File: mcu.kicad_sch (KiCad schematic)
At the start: 30 parts, among them J301 CONN_MCU_SERIAL, J302 EXT_CONN, SW301 SW_RST, SW302 SW_BOOT0, U301 STM32F765IITx, Y301 25MHz

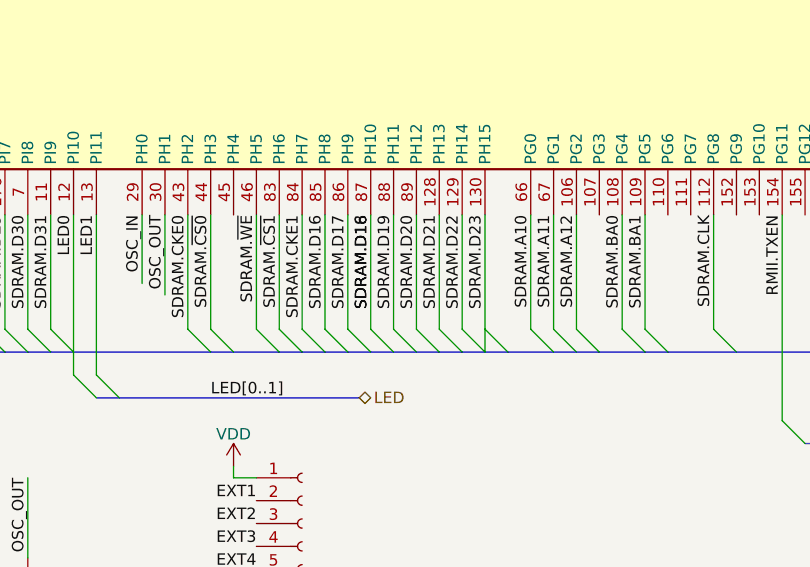
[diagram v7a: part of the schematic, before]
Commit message: Fix overlapped label on DRAM data bus causing D16 and D18 nets to be connected together.
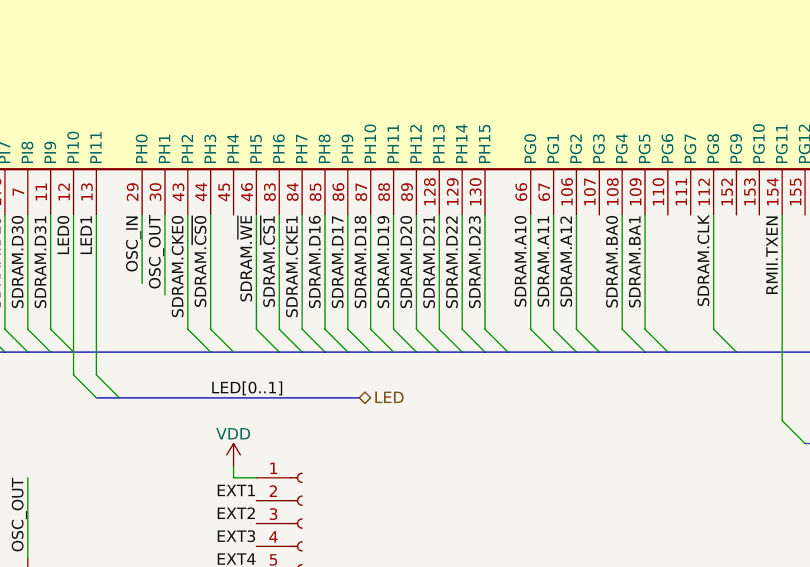
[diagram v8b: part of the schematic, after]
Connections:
- net SDRAM.D16: no longer U301.87 (PH10)
- new net SDRAM.D18: U301.87 (PH10)
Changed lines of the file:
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@@
-    (stroke (width 0) (type default) (color 0 0 0 0))
-  )
-  (bus_entry (at 158.75 137.16) (size 2.54 2.54)
     (stroke (width 0) (type default) (color 0 0 0 0))
   )
@@
     (stroke (width 0) (type default) (color 0 0 0 0))
   )
+  (bus_entry (at 161.29 139.7) (size -2.54 -2.54)
+    (stroke (width 0) (type default) (color 0 0 0 0))
+  )
   (bus_entry (at 128.27 137.16) (size 2.54 2.54)
     (stroke (width 0) (type default) (color 0 0 0 0))
@@
     (stroke (width 0) (type default) (color 0 0 0 0))
   )
+  (wire (pts (xy 158.75 124.46) (xy 158.75 137.16))
+    (stroke (width 0) (type default) (color 0 0 0 0))
+  )
   (wire (pts (xy 140.97 24.13) (xy 140.97 26.67))
     (stroke (width 0) (type default) (color 0 0 0 0))
@@
     (stroke (width 0) (type default) (color 0 0 0 0))
   )
+  (bus (pts (xy 161.29 139.7) (xy 163.83 139.7))
+    (stroke (width 0) (type default) (color 0 0 0 0))
+  )
   (bus (pts (xy 92.71 31.75) (xy 105.41 31.75))
     (stroke (width 0) (type default) (color 0 0 0 0))
@@
     (stroke (width 0) (type default) (color 0 0 0 0))
   )
-  (wire (pts (xy 158.75 124.46) (xy 158.75 137.16))
-    (stroke (width 0) (type default) (color 0 0 0 0))
-  )
   (bus (pts (xy 269.24 26.67) (xy 269.24 16.51))
     (stroke (width 0) (type default) (color 0 0 0 0))
@@
     (stroke (width 0) (type default) (color 0 0 0 0))
   )
-  (bus (pts (xy 161.29 139.7) (xy 163.83 139.7))
+  (bus (pts (xy 158.75 139.7) (xy 161.29 139.7))
     (stroke (width 0) (type default) (color 0 0 0 0))
   )
@@
     (stroke (width 0) (type default) (color 0 0 0 0))
   )
-  (bus (pts (xy 158.75 139.7) (xy 161.29 139.7))
-    (stroke (width 0) (type default) (color 0 0 0 0))
-  )
   (wire (pts (xy 41.91 88.9) (xy 44.45 88.9))
     (stroke (width 0) (type default) (color 0 0 0 0))
@@
     (stroke (width 0) (type default) (color 0 0 0 0))
   )
-  (wire (pts (xy 176.53 139.7) (xy 176.53 137.16))
-    (stroke (width 0) (type default) (color 0 0 0 0))
-  )
   (bus (pts (xy 184.15 26.67) (xy 186.69 26.67))
     (stroke (width 0) (type default) (color 0 0 0 0))
@@
     (stroke (width 0) (type default) (color 0 0 0 0))
   )
+  (label "JTAG.TCK" (at 87.63 50.8 90)
+    (effects (font (size 1.27 1.27)) (justify left bottom))
+  )
+  (label "SDMMC.CD" (at 153.67 50.8 90)
+    (effects (font (size 1.27 1.27)) (justify left bottom))
+  )
+  (label "SDRAM.CKE1" (at 156.21 124.46 270)
+    (effects (font (size 1.27 1.27)) (justify right bottom))
+  )
+  (label "SDRAM.~{CAS}" (at 219.71 124.46 270)
+    (effects (font (size 1.27 1.27)) (justify right bottom))
+  )
+  (label "EXT6" (at 113.03 50.8 90)
+    (effects (font (size 1.27 1.27)) (justify left bottom))
+  )
+  (label "SDRAM.A3" (at 232.41 124.46 270)
+    (effects (font (size 1.27 1.27)) (justify right bottom))
+  )
+  (label "SDRAM.CLK" (at 201.93 124.46 270)
+    (effects (font (size 1.27 1.27)) (justify right bottom))
+  )
+  (label "SDMMC.D3" (at 166.37 50.8 90)
+    (effects (font (size 1.27 1.27)) (justify left bottom))
+  )
+  (label "SDRAM.BA1" (at 194.31 124.46 270)
+    (effects (font (size 1.27 1.27)) (justify right bottom))
+  )
+  (label "SDRAM.D11" (at 260.35 50.8 90)
+    (effects (font (size 1.27 1.27)) (justify left bottom))
+  )
+  (label "RMII.LED" (at 97.79 50.8 90)
+    (effects (font (size 1.27 1.27)) (justify left bottom))
+  )
+  (label "BOOT0" (at 54.61 144.78 0)
+    (effects (font (size 1.27 1.27)) (justify left bottom))
+  )
+  (label "SDRAM.~{BL3}" (at 118.11 124.46 270)
+    (effects (font (size 1.27 1.27)) (justify right bottom))
+  )
   (label "SDRAM.D18" (at 163.83 124.46 270)
-    (effects (font (size 1.27 1.27)) (justify right bottom))
-  )
-  (label "JTAG.TCK" (at 87.63 50.8 90)
-    (effects (font (size 1.27 1.27)) (justify left bottom))
-  )
-  (label "SDMMC.CD" (at 153.67 50.8 90)
-    (effects (font (size 1.27 1.27)) (justify left bottom))
-  )
-  (label "SDRAM.CKE1" (at 156.21 124.46 270)
-    (effects (font (size 1.27 1.27)) (justify right bottom))
-  )
-  (label "SDRAM.~{CAS}" (at 219.71 124.46 270)
-    (effects (font (size 1.27 1.27)) (justify right bottom))
-  )
-  (label "EXT6" (at 113.03 50.8 90)
-    (effects (font (size 1.27 1.27)) (justify left bottom))
-  )
-  (label "SDRAM.A3" (at 232.41 124.46 270)
-    (effects (font (size 1.27 1.27)) (justify right bottom))
-  )
-  (label "SDRAM.CLK" (at 201.93 124.46 270)
-    (effects (font (size 1.27 1.27)) (justify right bottom))
-  )
-  (label "SDMMC.D3" (at 166.37 50.8 90)
-    (effects (font (size 1.27 1.27)) (justify left bottom))
-  )
-  (label "SDRAM.BA1" (at 194.31 124.46 270)
-    (effects (font (size 1.27 1.27)) (justify right bottom))
-  )
-  (label "SDRAM.D11" (at 260.35 50.8 90)
-    (effects (font (size 1.27 1.27)) (justify left bottom))
-  )
-  (label "RMII.LED" (at 97.79 50.8 90)
-    (effects (font (size 1.27 1.27)) (justify left bottom))
-  )
-  (label "BOOT0" (at 54.61 144.78 0)
-    (effects (font (size 1.27 1.27)) (justify left bottom))
-  )
-  (label "SDRAM.~{BL3}" (at 118.11 124.46 270)
-    (effects (font (size 1.27 1.27)) (justify right bottom))
-  )
-  (label "SDRAM.D16" (at 163.83 124.46 270)
     (effects (font (size 1.27 1.27)) (justify right bottom))
   )
@@
     (effects (font (size 1.27 1.27)) (justify right bottom))
   )
+  (label "SDRAM.D16" (at 158.75 124.46 270)
+    (effects (font (size 1.27 1.27)) (justify right bottom))
+  )
   (label "LED0" (at 130.81 124.46 270)
     (effects (font (size 1.27 1.27)) (justify right bottom))
@@
     (effects (font (size 1.27 1.27)) (justify left bottom))
   )
-  (label "SDRAM.D16" (at 158.75 124.46 270)
-    (effects (font (size 1.27 1.27)) (justify right bottom))
-  )
   (label "RMII.~{RST}" (at 95.25 50.8 90)
